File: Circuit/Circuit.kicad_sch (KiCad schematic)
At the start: 26 parts, among them J1 Conn_01x08_Socket, J2 Conn_01x08_Socket, Q2 S8050, Q3 S8050, Q4 S8550, Q5 IRFZ44n, SW1 SW_DPDT_x2, SW2 SW_DPDT_x2, U1 L7805

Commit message: finished circuit and started PCB
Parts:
- removed C1: C, symbol Device:C
- added Debug1: 1x3_Header, Connector_PinSocket_2.54mm:PinSocket_1x03_P2.54mm_Vertical, symbol Connector:Conn_01x03_Socket
- added R8: 10K, Resistor_THT:R_Axial_DIN0207_L6.3mm_D2.5mm_P7.62mm_Horizontal, symbol Device:R
- added SW3: SW_DPDT_x2, Connector_PinSocket_2.54mm:PinSocket_1x03_P2.54mm_Vertical, symbol Switch:SW_DPDT_x2
- C1: renamed from C2; value C_Polarized -> 300uF; footprint (none) -> Capacitor_THT:CP_Radial_D8.0mm_P3.80mm
- ESP32-CAM1: renamed from J1; value Conn_01x08_Socket -> 01x08_Header
- ESP32-CAM2: renamed from J2; value Conn_01x08_Socket -> 01x08_Header
- MotorOutput1: renamed from MotorOutput; value Conn_01x02_Socket -> TerminalBlock
- Power24V1: renamed from Power24V; value Conn_01x02_Socket -> TerminalBlock
- SW1, SW2: footprint Button_Switch_THT:SW_Slide-03_Wuerth-WS-SLTV_10x2.5x6.4_P2.54mm -> Connector_PinSocket_2.54mm:PinSocket_1x03_P2.54mm_Vertical
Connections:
- net +5V: now also C1.1, ESP32-CAM1.1 (Pin_1), R4.2, R8.2
- net GND: now also C1.2, ESP32-CAM2.8 (Pin_8), Debug1.3 (Pin_3), SW3.1 (A)
- net GREEN_LED: now also ESP32-CAM1.5 (Pin_5)
- net MotorPWM: now also ESP32-CAM2.2 (Pin_2)
- net POT_ADC: now also ESP32-CAM1.8 (Pin_8), RV1.2
- net RED_LED: now also ESP32-CAM1.3 (Pin_3)
- net SWITCH1: now also ESP32-CAM1.6 (Pin_6)
- net SWITCH2: now also ESP32-CAM1.7 (Pin_7)
- net YELLOW_LED: now also ESP32-CAM1.4 (Pin_4)
- net BOOT_MODE: now reaches ESP32-CAM2.3 (Pin_3)
- net BOOT_MODE: now also SW3.2 (B)
- net RX: now reaches ESP32-CAM2.6 (Pin_6)
- net RX: now also Debug1.1 (Pin_1)
- net TX: now reaches ESP32-CAM2.7 (Pin_7)
- net TX: now also Debug1.2 (Pin_2)
- net at RV1.1: now also R4.1
- new net: R8.1, SW3.3 (C)
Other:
- moved on the sheet: C1, D1, D2, D3, D4, MotorOutput1, Power24V1, Q2, Q3, Q4, Q5, R1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

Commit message: finished PCB
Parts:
- removed D4: SR360, Diode_THT:D_DO-27_P12.70mm_Horizontal, symbol Device:D
- removed MotorOutput1: TerminalBlock, TerminalBlock:TerminalBlock_bornier-2_P5.08mm, symbol Connector:Conn_01x02_Socket
- removed Q2, Q3: S8050, Package_TO_SOT_THT:TO-92_Inline, symbol Transistor_BJT:S8050
- removed Q4: S8550, Package_TO_SOT_THT:TO-92_Inline, symbol Transistor_BJT:S8550
- removed Q5: IRFZ44n, Package_TO_SOT_THT:TO-220-3_Vertical, symbol Transistor_FET:IRF540N
- removed R7: 10k, Resistor_THT:R_Axial_DIN0207_L6.3mm_D2.5mm_P7.62mm_Horizontal, symbol Device:R
- removed R9: 1k, Resistor_THT:R_Axial_DIN0207_L6.3mm_D2.5mm_P7.62mm_Horizontal, symbol Device:R
- added MotorControl1: JST-2P, Connector_JST:JST_EH_B2B-EH-A_1x02_P2.50mm_Vertical, symbol Connector:Conn_01x02_Socket
- D1: value LED -> RED
- D2: value LED -> YELLOW
- D3: value LED -> GREEN
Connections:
- net +5V: now also ESP32-CAM2.8 (Pin_8); no longer ESP32-CAM1.1 (Pin_1)
- net BOOT_MODE: now also ESP32-CAM1.6 (Pin_6); no longer ESP32-CAM2.3 (Pin_3)
- net GND: now also ESP32-CAM1.1 (Pin_1), RV1.1, MotorControl1.2 (Pin_2); no longer ESP32-CAM2.8 (Pin_8), RV1.3
- net GREEN_LED: now also ESP32-CAM2.3 (Pin_3); no longer ESP32-CAM1.5 (Pin_5)
- net MotorPWM: now also ESP32-CAM1.7 (Pin_7), MotorControl1.1 (Pin_1); no longer ESP32-CAM2.2 (Pin_2)
- net POT_ADC: now also ESP32-CAM2.6 (Pin_6); no longer ESP32-CAM1.8 (Pin_8)
- net RED_LED: now also ESP32-CAM2.4 (Pin_4); no longer ESP32-CAM1.3 (Pin_3)
- net RX: now also ESP32-CAM1.3 (Pin_3); no longer ESP32-CAM2.6 (Pin_6)
- net SWITCH1: now also ESP32-CAM2.1 (Pin_1); no longer ESP32-CAM1.6 (Pin_6)
- net SWITCH2: now also ESP32-CAM2.2 (Pin_2); no longer ESP32-CAM1.7 (Pin_7)
- net TX: now also ESP32-CAM1.2 (Pin_2); no longer ESP32-CAM2.7 (Pin_7)
- net YELLOW_LED: now also ESP32-CAM2.5 (Pin_5); no longer ESP32-CAM1.4 (Pin_4)
- net at R4.1: now also RV1.3; no longer RV1.1
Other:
- moved on the sheet: ESP32-CAM1, ESP32-CAM2, R4, R5, R6, R8, RV1, SW1A, SW2A, SW3A

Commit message: fixed PCB, started programming
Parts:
- removed R6: 10K, Resistor_THT:R_Axial_DIN0207_L6.3mm_D2.5mm_P7.62mm_Horizontal, symbol Device:R
- removed SW2: SW_DPDT_x2, Connector_PinSocket_2.54mm:PinSocket_1x03_P2.54mm_Vertical, symbol Switch:SW_DPDT_x2
- added Proximity1: JST-3p, Connector_JST:JST_EH_B3B-EH-A_1x03_P2.50mm_Vertical, symbol Connector:Conn_01x03_Socket
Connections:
- net +5V: now also Proximity1.1 (Pin_1)
- net GND: now also Proximity1.2 (Pin_2)
- net SWITCH2 renamed Proximity
- net Proximity: now also Proximity1.3 (Pin_3)

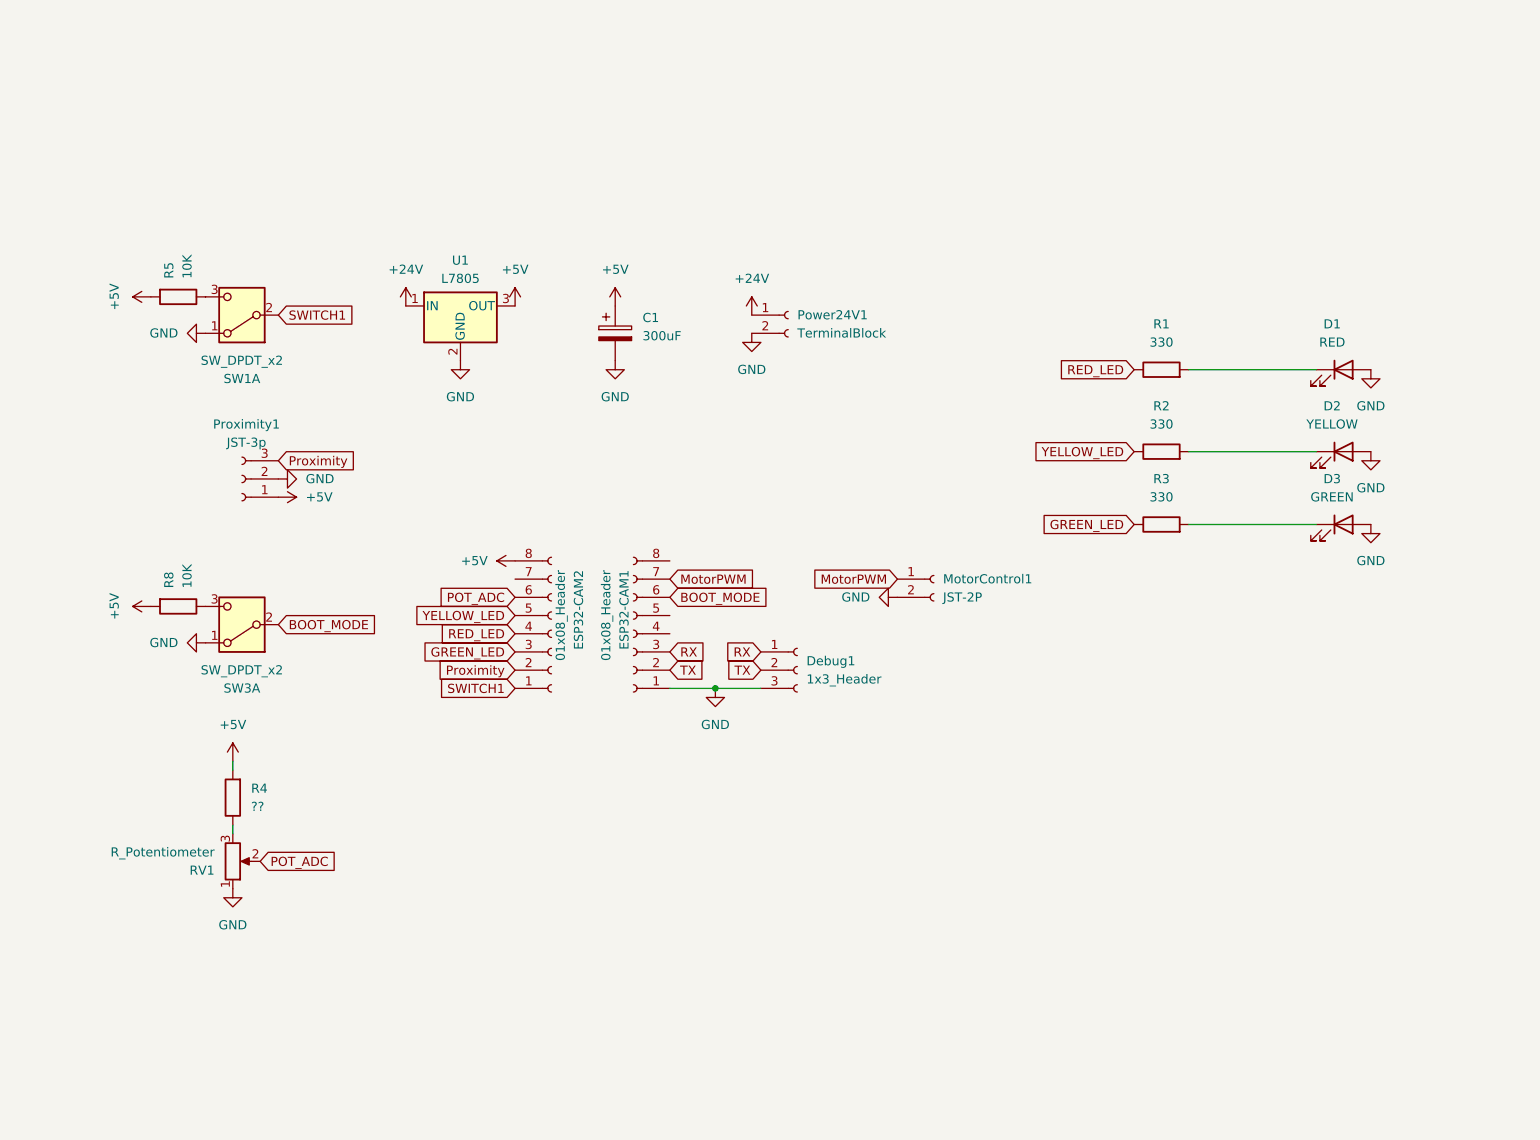
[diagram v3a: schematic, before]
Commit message: finished Interfacing all sensors and actuators, pending server code
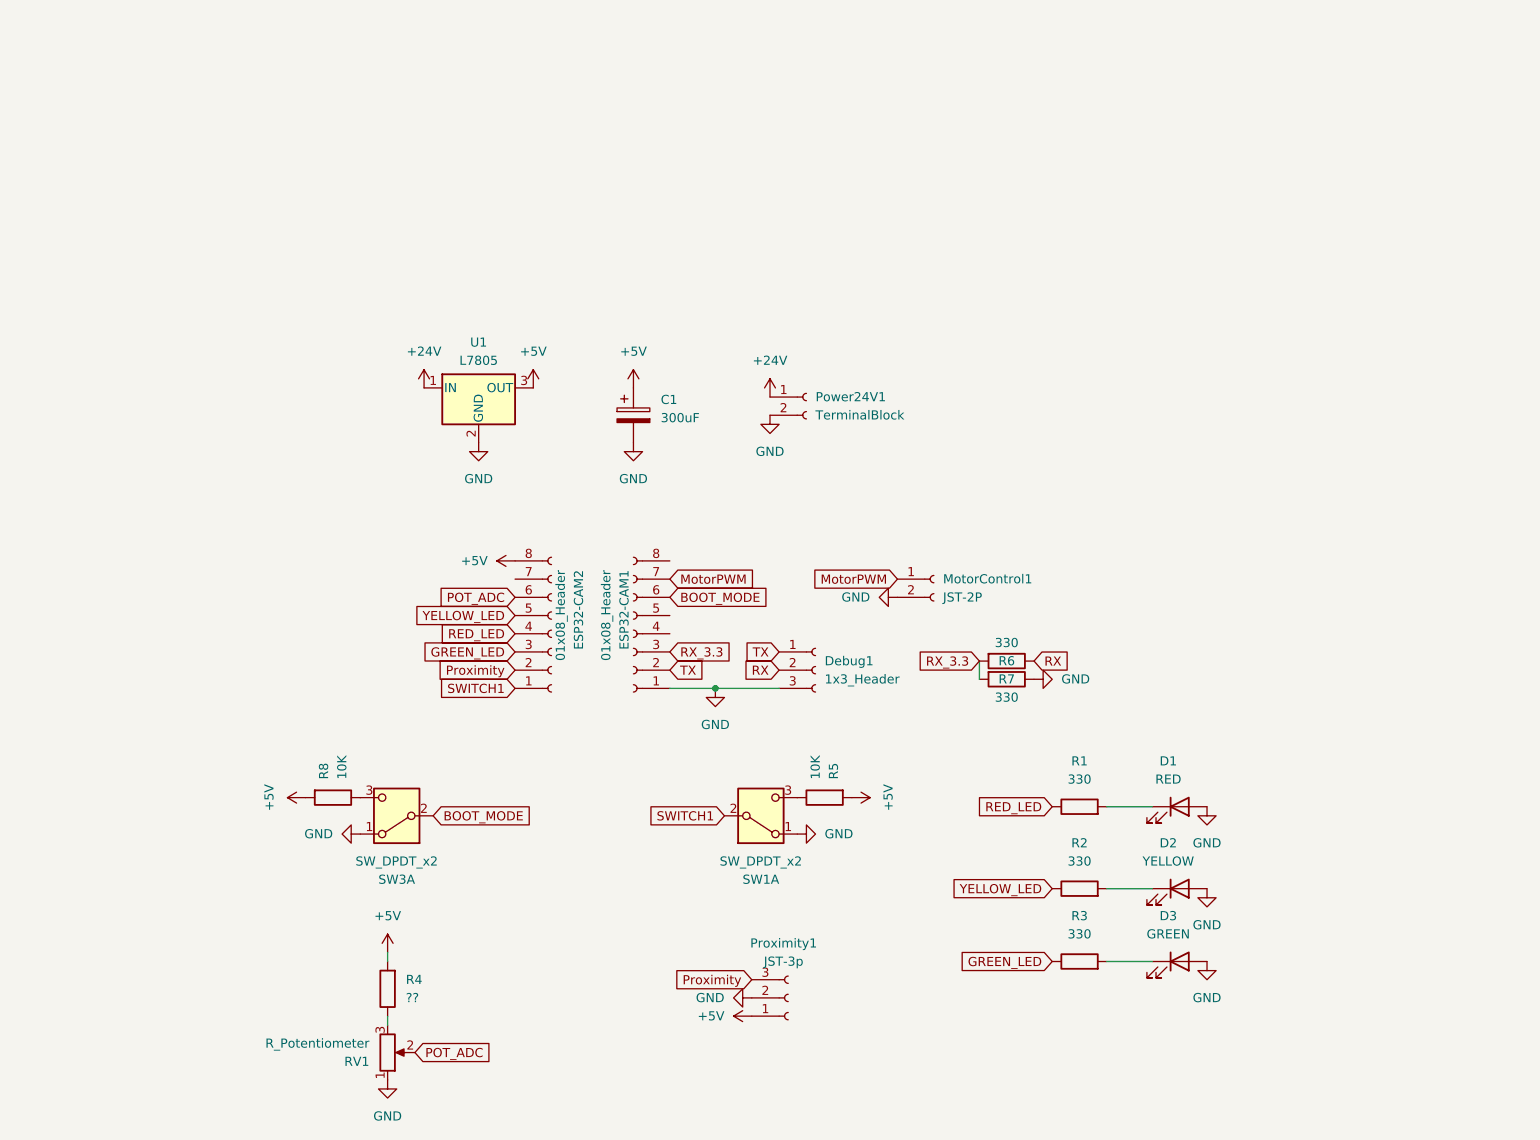
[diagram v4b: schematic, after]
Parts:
- added R6, R7: 330, Resistor_THT:R_Axial_DIN0207_L6.3mm_D2.5mm_P7.62mm_Horizontal, symbol Device:R
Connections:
- net GND: now also R7.1
- net RX: now also Debug1.2 (Pin_2), R6.1; no longer Debug1.1 (Pin_1), ESP32-CAM1.3 (Pin_3)
- net TX: now also Debug1.1 (Pin_1); no longer Debug1.2 (Pin_2)
- new net RX_3.3: ESP32-CAM1.3 (Pin_3), R6.2, R7.2
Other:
- moved on the sheet: C1, D1, D2, D3, Debug1, Power24V1, Proximity1, R1, R2, R3, R4, R5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

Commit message: schematic and PCB modification Done
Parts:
- removed MotorControl1: JST-2P, Connector_JST:JST_EH_B2B-EH-A_1x02_P2.50mm_Vertical, symbol Connector:Conn_01x02_Socket
- removed RV1: R_Potentiometer, Potentiometer_THT:Potentiometer_Alps_RK163_Single_Horizontal, symbol Device:R_Potentiometer
- removed SW3: SW_DPDT_x2, Connector_PinSocket_2.54mm:PinSocket_1x03_P2.54mm_Vertical, symbol Switch:SW_DPDT_x2
- added Motor1: JST 4P, Connector_JST:JST_EH_B4B-EH-A_1x04_P2.50mm_Vertical, symbol Connector:Conn_01x04_Socket
- added Q1: S8050, Package_TO_SOT_THT:TO-92_Inline_Wide, symbol Transistor_BJT:S8050
- added R10: 2k, Resistor_THT:R_Axial_DIN0207_L6.3mm_D2.5mm_P7.62mm_Horizontal, symbol Device:R
- added R9: 1k, Resistor_THT:R_Axial_DIN0207_L6.3mm_D2.5mm_P7.62mm_Horizontal, symbol Device:R
- Proximity1: value JST-3p -> JST 3P
- R4: value ?? -> 1k
- R6: value 330 -> 1k
- R7: value 330 -> 2k
- R8: value 10K -> 2k
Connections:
- net POT_ADC is gone; now on net GREEN_LED: ESP32-CAM2.6 (Pin_6)
- net +5V: no longer R4.2
- net BOOT_MODE: now also SW1.2 (B)
- net GND: now also Motor1.4 (Pin_4), Q1.1 (E), R10.1
- net GREEN_LED: no longer ESP32-CAM2.3 (Pin_3)
- net MotorPWM: now also ESP32-CAM2.3 (Pin_3), Motor1.3 (Pin_3); no longer ESP32-CAM1.7 (Pin_7)
- net Proximity: now also ESP32-CAM2.1 (Pin_1), R4.1, R10.2; no longer ESP32-CAM2.2 (Pin_2), Proximity1.3 (Pin_3)
- net MotorDir2: now reaches R8.1
- net MotorDir2: now also Motor1.1 (Pin_1), Q1.3 (C)
- removed net SWITCH1: ESP32-CAM2.1 (Pin_1), SW1.2 (B)
- new net: Q1.2 (B), R9.2
- new net: Proximity1.3 (Pin_3), R4.2
- new net MotorDir1: ESP32-CAM2.2 (Pin_2), Motor1.2 (Pin_2), R9.1
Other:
- moved on the sheet: D1, D2, D3, Proximity1, R1, R2, R3, R5, SW1A
